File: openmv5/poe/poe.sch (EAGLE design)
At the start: 47 parts, among them IC1 AG9905LP, J1 GMJXHT-MM-S-88, T1 PT61018PEL, U1 OPENMV5-BOTTOM

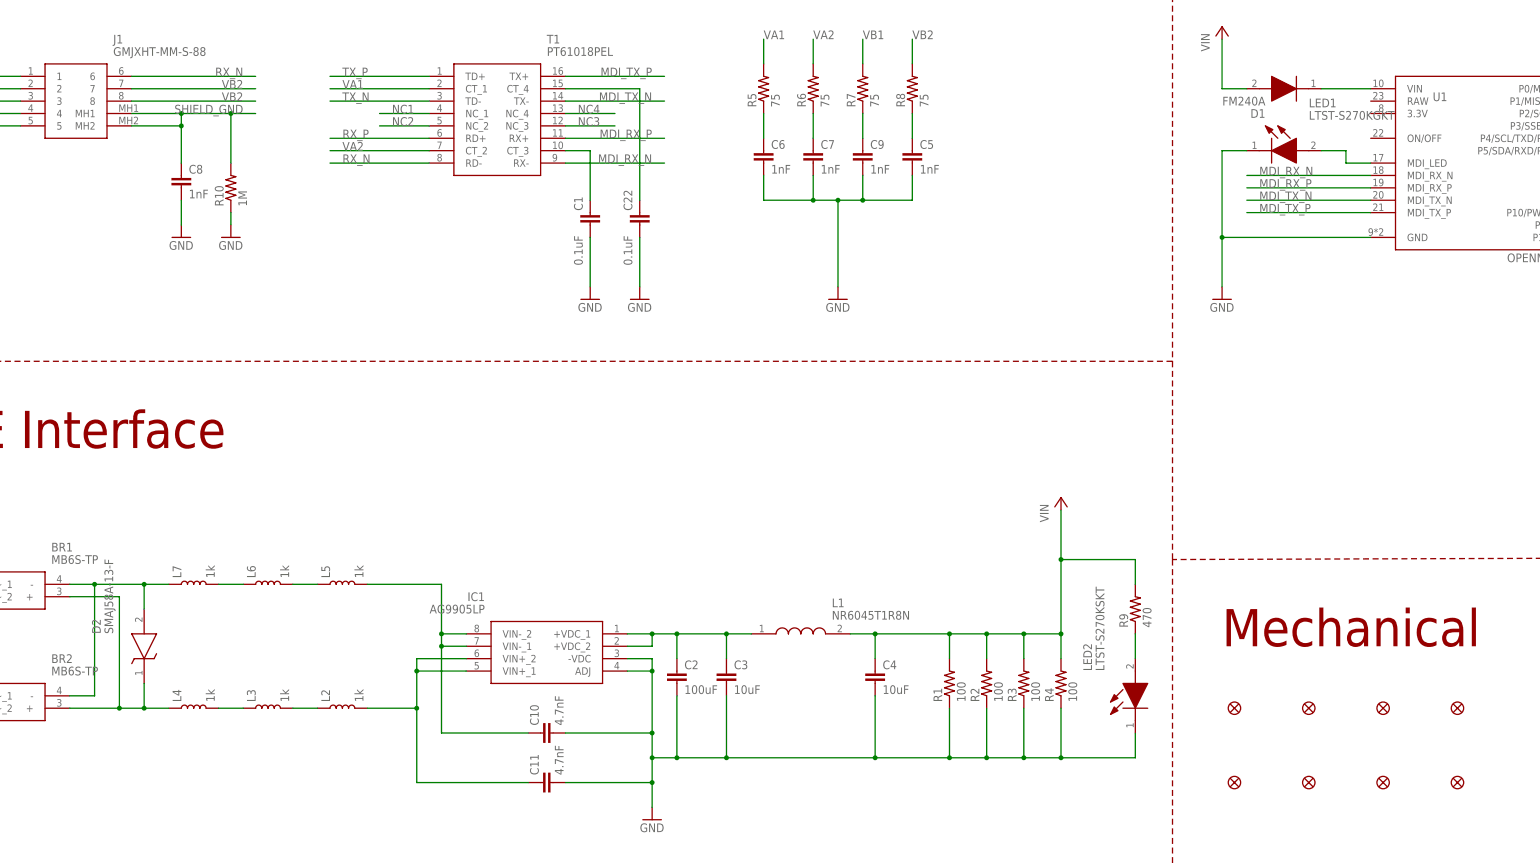
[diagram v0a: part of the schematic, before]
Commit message: Add labels to PoE shield
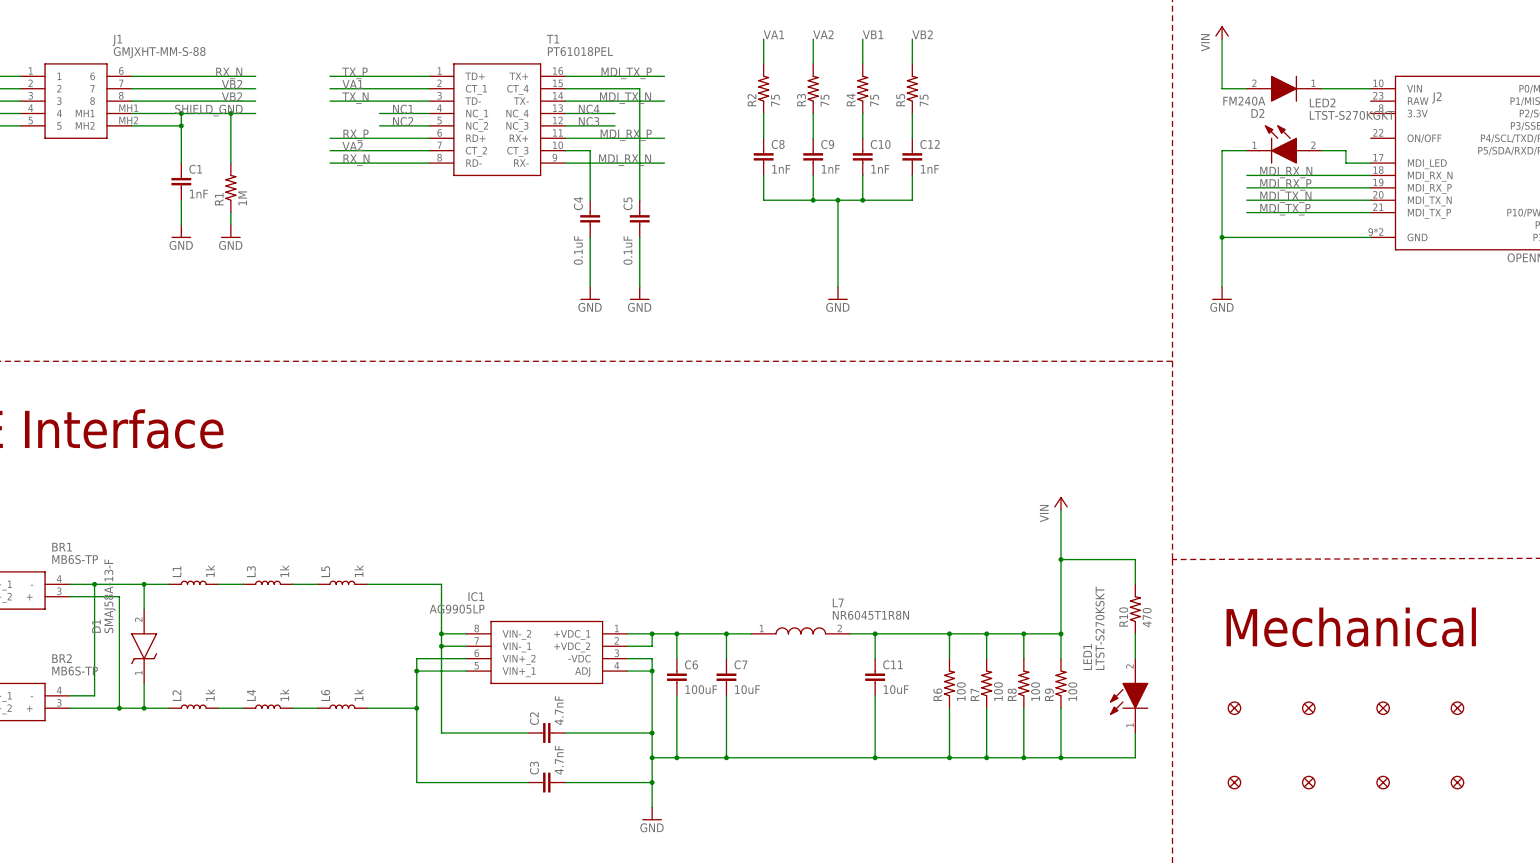
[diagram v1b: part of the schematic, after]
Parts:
- removed C22: 0.1uF, rcl:C-EUC0201
- added C12: 1nF, rcl:C-EUC1206
- C1: value 0.1uF -> 1nF; device rcl:C-EUC0201 -> rcl:C-EUC1206; MPN CL03A104KQ3NNNC -> 1206B102K252CT
- C10: value 4.7nF -> 1nF; device rcl:C-EUC1812 -> rcl:C-EUC1206; MPN 202S43W472KV4E -> 1206B102K252CT
- C11: value 4.7nF -> 10uF; device rcl:C-EUC1812 -> rcl:C-EUC0402; MPN 202S43W472KV4E -> GRM155R60J106ME05D
- C2: value 100uF -> 4.7nF; device rcl:C-EUC1206 -> rcl:C-EUC1812; MPN CL31A107MQHNNWE -> 202S43W472KV4E
- C3: value 10uF -> 4.7nF; device rcl:C-EUC0402 -> rcl:C-EUC1812; MPN GRM155R60J106ME05D -> 202S43W472KV4E
- C4: value 10uF -> 0.1uF; device rcl:C-EUC0402 -> rcl:C-EUC0201; MPN GRM155R60J106ME05D -> CL03A104KQ3NNNC
- C5: value 1nF -> 0.1uF; device rcl:C-EUC1206 -> rcl:C-EUC0201; MPN 1206B102K252CT -> CL03A104KQ3NNNC
- C6: value 1nF -> 100uF; MPN 1206B102K252CT -> CL31A107MQHNNWE
- C7: value 1nF -> 10uF; device rcl:C-EUC1206 -> rcl:C-EUC0402; MPN 1206B102K252CT -> GRM155R60J106ME05D
- D1: value FM240A -> SMAJ58A-13-F; device FM240A:FM240A -> SMAJ58A-13-F:SMAJ58A-13-F; MPN FM240A -> SMAJ58A/TR13
- D2: value SMAJ58A-13-F -> FM240A; device SMAJ58A-13-F:SMAJ58A-13-F -> FM240A:FM240A; MPN SMAJ58A/TR13 -> FM240A
- L1: value NR6045T1R8N -> 1k; device NR6045T1R8N:NR6045T1R8N -> SparkFun-Coils:INDUCTOR-0402-3.9NH; MPN NR6045T1R8N -> BBPY00100505102Y00
- L7: value 1k -> NR6045T1R8N; device SparkFun-Coils:INDUCTOR-0402-3.9NH -> NR6045T1R8N:NR6045T1R8N; MPN BBPY00100505102Y00 -> NR6045T1R8N
- LED1: value LTST-S270KGKT -> LTST-S270KSKT; device LTST-S270K:LTST-S270KGKT -> LTST-S270K:LTST-S270KSKT; MPN LTST-S270KGKT -> LTST-S270KSKT
- LED2: value LTST-S270KSKT -> LTST-S270KGKT; device LTST-S270K:LTST-S270KSKT -> LTST-S270K:LTST-S270KGKT; MPN LTST-S270KSKT -> LTST-S270KGKT
- R1: value 100 -> 1M; device rcl:R-US_R2512 -> rcl:R-US_R1206; MPN RC2512JK-07100RL -> RMCF1206FT1M00
- R10: value 1M -> 470; device rcl:R-US_R1206 -> rcl:R-US_R0603; MPN RMCF1206FT1M00 -> 0603WAJ0471T5E
- R2, R3, R4: value 100 -> 75; device rcl:R-US_R2512 -> rcl:R-US_R0402; MPN RC2512JK-07100RL -> 0402WGF750JTCE
- R6, R7, R8: value 75 -> 100; device rcl:R-US_R0402 -> rcl:R-US_R2512; MPN 0402WGF750JTCE -> RC2512JK-07100RL
- R9: value 470 -> 100; device rcl:R-US_R0603 -> rcl:R-US_R2512; MPN 0603WAJ0471T5E -> RC2512JK-07100RL
- renumbered U1 to J2
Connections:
- net GND: now also C12.2, R6.1, R7.1, R8.1, R9.1; no longer C22.2, R10.1, R2.1, R3.1, R4.1
- net MDI_LED: now also LED2.A; no longer LED1.A
- net MDI_RX_CT: now also C4.1; no longer C1.1
- net MDI_TX_CT: now also C5.1; no longer C22.1
- net POE_VIN_INT_N: now also C2.1; no longer C10.1
- net POE_VIN_INT_P: now also C3.1, L6.2; no longer C11.1, L2.2
- net POE_VIN_N: now also D1.A, L1.1; no longer D2.A, L7.1
- net POE_VIN_N0: now also L1.2, L3.1; no longer L6.1, L7.2
- net POE_VIN_N1: now also L3.2; no longer L6.2
- net POE_VIN_P: now also D1.K, L2.1; no longer D2.K, L4.1
- net POE_VIN_P0: now also L2.2, L4.1; no longer L3.1, L4.2
- net POE_VIN_P1: now also L4.2, L6.1; no longer L2.1, L3.2
- net SHIELD_GND: now also C1.1, R1.2; no longer C8.1, R10.2
- net VA1: now also R2.2; no longer R5.2
- net VA1_ISO: now also C8.1, R2.1; no longer C6.1, R5.1
- net VA2: now also R3.2; no longer R6.2
- net VA2_ISO: now also C9.1, R3.1; no longer C7.1, R6.1
- net VB1: now also R4.2; no longer R7.2
- net VB1_ISO: now also C10.1, R4.1; no longer C9.1, R7.1
- net VB2: now also R5.2; no longer R8.2
- net VB2_ISO: now also C12.1, R5.1; no longer C5.1, R8.1
- net VDC: now also C6.1, C7.1, L7.1; no longer C2.1, C3.1, L1.1
- net VIN: now also C11.1, D2.A, L7.2, R10.2, R6.2, R7.2, R8.2; no longer C4.1, D1.A, L1.2, R1.2, R2.2, R3.2, R4.2
- net VIN_INT: now also D2.K; no longer D1.K
- net VIN_LED: now also LED1.A, R10.1; no longer LED2.A, R9.1
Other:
- moved on the sheet: C1, C10, C11, C2, C3, C4, C5, C6, C7, C8, C9, L2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

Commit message: Update part
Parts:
- R10: MPN 0603WAJ0471T5E -> CR0603-FX-4700ELF
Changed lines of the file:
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@@
 </pinmapping>
 </spice>
-<attribute name="MPN" value="0603WAJ0471T5E"/>
+<attribute name="MPN" value="CR0603-FX-4700ELF"/>
 </part>
 <part name="D1" library="SMAJ58A-13-F" deviceset="SMAJ58A-13-F" device="">

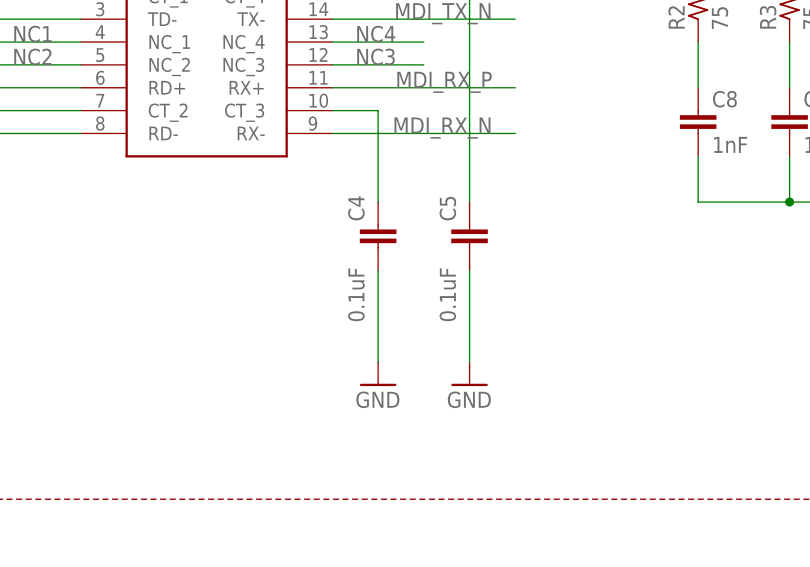
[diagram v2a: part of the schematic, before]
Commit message: Remove 0201 components
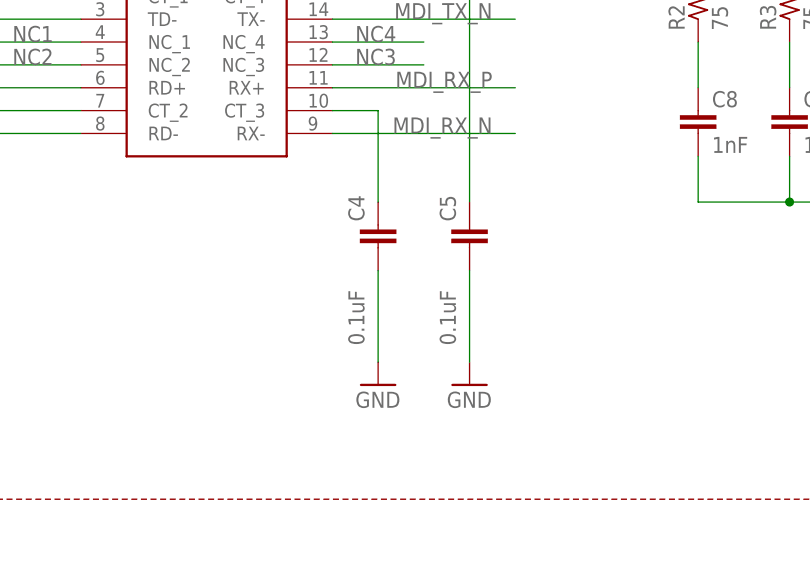
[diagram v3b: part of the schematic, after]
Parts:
- C4, C5: device rcl:C-EUC0201 -> SparkFun-Capacitors:0.1UF-0402-16V-10%; MPN CL03A104KQ3NNNC -> GRM155R71H104KE14D
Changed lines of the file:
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@@
 <attribute name="MPN" value="PT61018PEL"/>
 </part>
-<part name="C5" library="rcl" library_urn="urn:adsk.eagle:library:334" deviceset="C-EU" device="C0201" package3d_urn="urn:adsk.eagle:package:23690/2" value="0.1uF">
-<attribute name="MPN" value="CL03A104KQ3NNNC"/>
-</part>
-<part name="C4" library="rcl" library_urn="urn:adsk.eagle:library:334" deviceset="C-EU" device="C0201" package3d_urn="urn:adsk.eagle:package:23690/2" value="0.1uF">
-<attribute name="MPN" value="CL03A104KQ3NNNC"/>
+<part name="C5" library="SparkFun-Capacitors" library_urn="urn:adsk.eagle:library:510" deviceset="0.1UF" device="-0402-16V-10%" package3d_urn="urn:adsk.eagle:package:37413/1" value="0.1uF">
+<attribute name="MPN" value="GRM155R71H104KE14D"/>
+</part>
+<part name="C4" library="SparkFun-Capacitors" library_urn="urn:adsk.eagle:library:510" deviceset="0.1UF" device="-0402-16V-10%" package3d_urn="urn:adsk.eagle:package:37413/1" value="0.1uF">
+<attribute name="MPN" value="GRM155R71H104KE14D"/>
 </part>
 <part name="GND1" library="supply1" library_urn="urn:adsk.eagle:library:371" deviceset="GND" device=""/>
@@
 <attribute name="MPN" x="119.38" y="236.22" size="1.778" layer="96" display="off"/>
 </instance>
-<instance part="C5" gate="G$1" x="162.56" y="208.28" smashed="yes" rot="MR0">
+<instance part="C5" gate="G$1" x="162.56" y="205.74" smashed="yes" rot="MR0">
 <attribute name="NAME" x="161.036" y="208.661" size="1.778" layer="95" rot="R90"/>
-<attribute name="VALUE" x="161.036" y="203.581" size="1.778" layer="96" rot="MR270"/>
-<attribute name="MPN" x="162.56" y="208.28" size="1.778" layer="96" rot="MR0" display="off"/>
-</instance>
-<instance part="C4" gate="G$1" x="152.4" y="208.28" smashed="yes" rot="MR0">
+<attribute name="VALUE" x="161.036" y="201.041" size="1.778" layer="96" rot="MR270"/>
+<attribute name="MPN" x="162.56" y="205.74" size="1.778" layer="96" rot="MR0" display="off"/>
+</instance>
+<instance part="C4" gate="G$1" x="152.4" y="205.74" smashed="yes" rot="MR0">
 <attribute name="NAME" x="150.876" y="208.661" size="1.778" layer="95" rot="R90"/>
-<attribute name="VALUE" x="150.876" y="203.581" size="1.778" layer="96" rot="MR270"/>
-<attribute name="MPN" x="152.4" y="208.28" size="1.778" layer="96" rot="MR0" display="off"/>
+<attribute name="VALUE" x="150.876" y="201.041" size="1.778" layer="96" rot="MR270"/>
+<attribute name="MPN" x="152.4" y="205.74" size="1.778" layer="96" rot="MR0" display="off"/>
 </instance>
 <instance part="GND1" gate="1" x="152.4" y="190.5" smashed="yes">

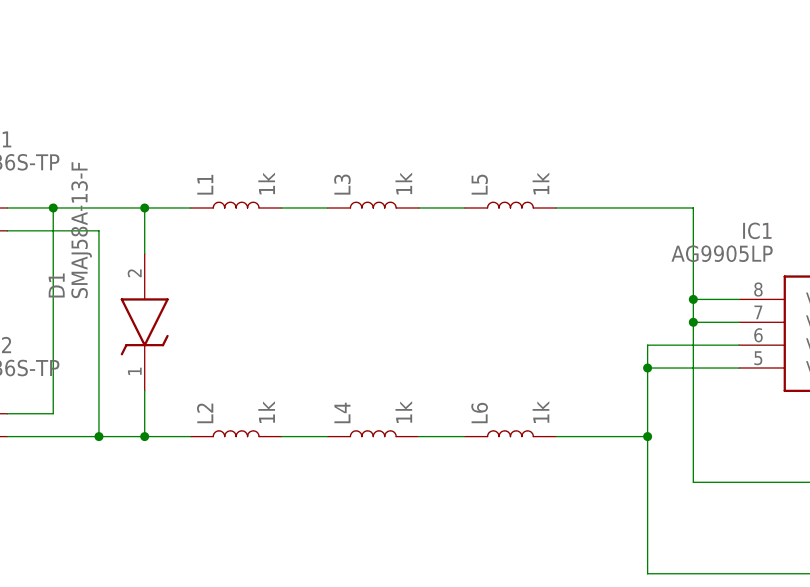
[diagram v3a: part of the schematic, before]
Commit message: Fix inductor size
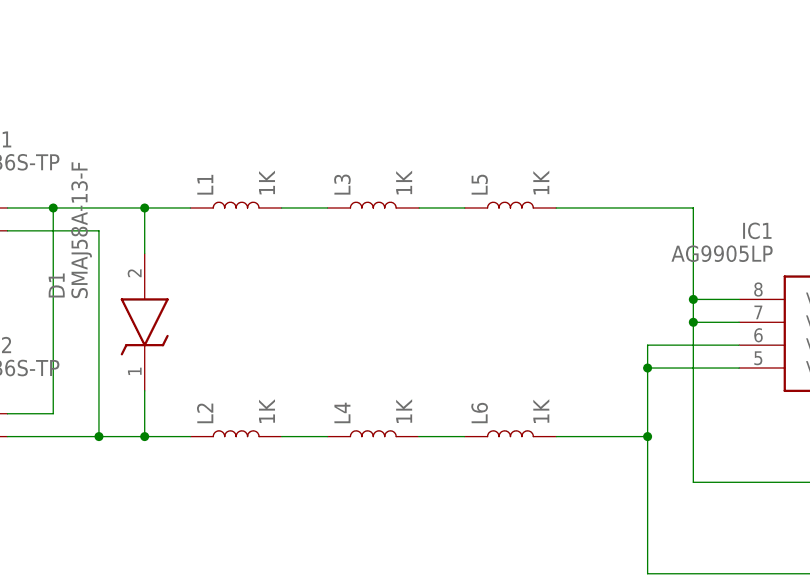
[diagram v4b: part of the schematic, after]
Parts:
- L1, L2, L3, L4, L5, L6: value 1k -> 1K; device SparkFun-Coils:INDUCTOR-0402-3.9NH -> SparkFun-Coils:INDUCTOR-0805-3.3UH
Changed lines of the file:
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@@
 <attribute name="MPN" value="202S43W472KV4E"/>
 </part>
-<part name="L6" library="SparkFun-Coils" library_urn="urn:adsk.eagle:library:512" deviceset="INDUCTOR" device="-0402-3.9NH" package3d_urn="urn:adsk.eagle:package:37575/1" value="1k">
+<part name="L6" library="SparkFun-Coils" library_urn="urn:adsk.eagle:library:512" deviceset="INDUCTOR" device="-0805-3.3UH" package3d_urn="urn:adsk.eagle:package:37579/1" value="1K">
 <attribute name="MPN" value="BBPY00100505102Y00"/>
 </part>
-<part name="L4" library="SparkFun-Coils" library_urn="urn:adsk.eagle:library:512" deviceset="INDUCTOR" device="-0402-3.9NH" package3d_urn="urn:adsk.eagle:package:37575/1" value="1k">
+<part name="L4" library="SparkFun-Coils" library_urn="urn:adsk.eagle:library:512" deviceset="INDUCTOR" device="-0805-3.3UH" package3d_urn="urn:adsk.eagle:package:37579/1" value="1K">
 <attribute name="MPN" value="BBPY00100505102Y00"/>
 </part>
-<part name="L2" library="SparkFun-Coils" library_urn="urn:adsk.eagle:library:512" deviceset="INDUCTOR" device="-0402-3.9NH" package3d_urn="urn:adsk.eagle:package:37575/1" value="1k">
+<part name="L2" library="SparkFun-Coils" library_urn="urn:adsk.eagle:library:512" deviceset="INDUCTOR" device="-0805-3.3UH" package3d_urn="urn:adsk.eagle:package:37579/1" value="1K">
 <attribute name="MPN" value="BBPY00100505102Y00"/>
 </part>
-<part name="L5" library="SparkFun-Coils" library_urn="urn:adsk.eagle:library:512" deviceset="INDUCTOR" device="-0402-3.9NH" package3d_urn="urn:adsk.eagle:package:37575/1" value="1k">
+<part name="L5" library="SparkFun-Coils" library_urn="urn:adsk.eagle:library:512" deviceset="INDUCTOR" device="-0805-3.3UH" package3d_urn="urn:adsk.eagle:package:37579/1" value="1K">
 <attribute name="MPN" value="BBPY00100505102Y00"/>
 </part>
-<part name="L3" library="SparkFun-Coils" library_urn="urn:adsk.eagle:library:512" deviceset="INDUCTOR" device="-0402-3.9NH" package3d_urn="urn:adsk.eagle:package:37575/1" value="1k">
+<part name="L3" library="SparkFun-Coils" library_urn="urn:adsk.eagle:library:512" deviceset="INDUCTOR" device="-0805-3.3UH" package3d_urn="urn:adsk.eagle:package:37579/1" value="1K">
 <attribute name="MPN" value="BBPY00100505102Y00"/>
 </part>
-<part name="L1" library="SparkFun-Coils" library_urn="urn:adsk.eagle:library:512" deviceset="INDUCTOR" device="-0402-3.9NH" package3d_urn="urn:adsk.eagle:package:37575/1" value="1k">
+<part name="L1" library="SparkFun-Coils" library_urn="urn:adsk.eagle:library:512" deviceset="INDUCTOR" device="-0805-3.3UH" package3d_urn="urn:adsk.eagle:package:37579/1" value="1K">
 <attribute name="MPN" value="BBPY00100505102Y00"/>
 </part>

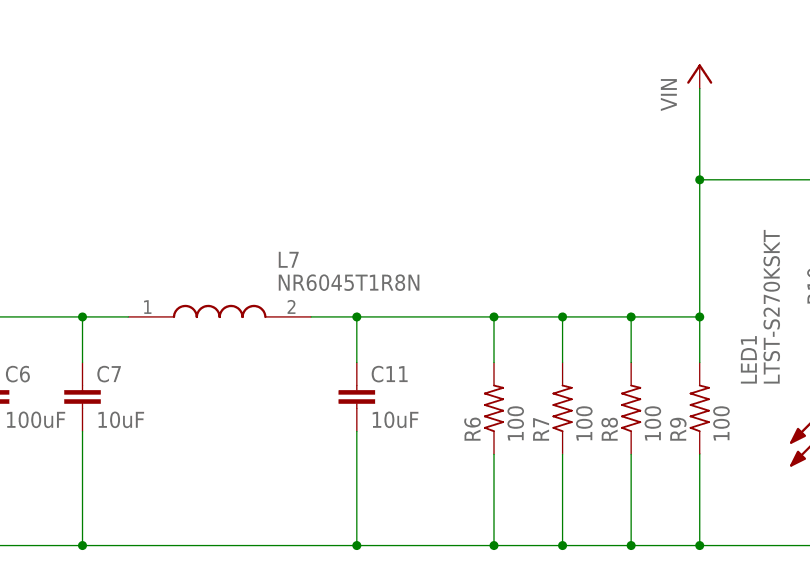
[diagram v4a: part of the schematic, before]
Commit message: Change inductor to something smaller
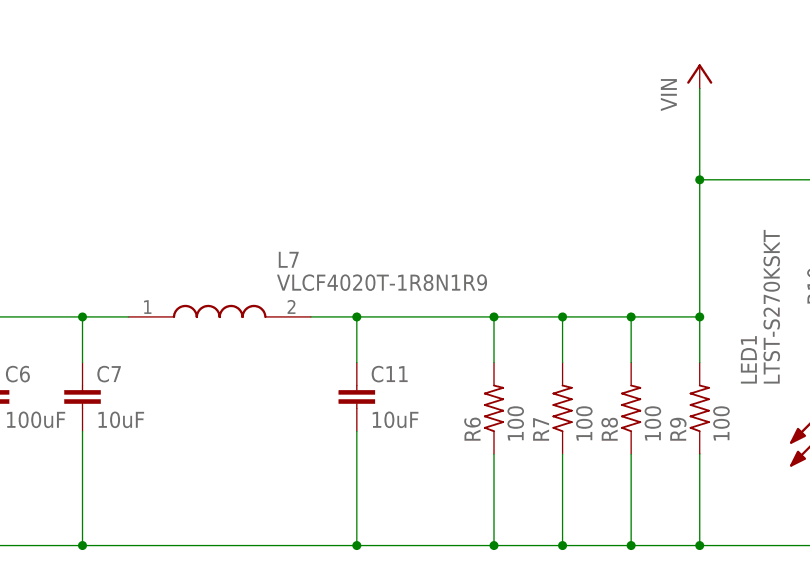
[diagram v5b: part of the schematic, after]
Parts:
- L7: value NR6045T1R8N -> VLCF4020T-1R8N1R9; device NR6045T1R8N:NR6045T1R8N -> VLCF4020T-1R8N1R9:VLCF4020T-1R8N1R9; MPN NR6045T1R8N -> VLCF4020T-1R8N1R9
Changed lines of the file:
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@@
 </part>
 <part name="GND3" library="supply1" library_urn="urn:adsk.eagle:library:371" deviceset="GND" device=""/>
-<part name="L7" library="NR6045T1R8N" deviceset="NR6045T1R8N" device="">
-<attribute name="MPN" value="NR6045T1R8N"/>
+<part name="L7" library="VLCF4020T-1R8N1R9" deviceset="VLCF4020T-1R8N1R9" device="">
+<attribute name="MPN" value="VLCF4020T-1R8N1R9"/>
 </part>
 <part name="C7" library="rcl" library_urn="urn:adsk.eagle:library:334" deviceset="C-EU" device="C0402" package3d_urn="urn:adsk.eagle:package:23626/2" value="10uF">

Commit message: Fix part and add 3D
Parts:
- R2, R3, R4, R5: MPN 0402WGF750JTCE -> CR0402-FX-75R0GLF
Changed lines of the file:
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@@
 </pinmapping>
 </spice>
-<attribute name="MPN" value="0402WGF750JTCE"/>
+<attribute name="MPN" value="CR0402-FX-75R0GLF"/>
 </part>
 <part name="R3" library="rcl" library_urn="urn:adsk.eagle:library:334" deviceset="R-US_" device="R0402" package3d_urn="urn:adsk.eagle:package:23547/3" value="75">
@@
 </pinmapping>
 </spice>
-<attribute name="MPN" value="0402WGF750JTCE"/>
+<attribute name="MPN" value="CR0402-FX-75R0GLF"/>
 </part>
 <part name="R4" library="rcl" library_urn="urn:adsk.eagle:library:334" deviceset="R-US_" device="R0402" package3d_urn="urn:adsk.eagle:package:23547/3" value="75">
@@
 </pinmapping>
 </spice>
-<attribute name="MPN" value="0402WGF750JTCE"/>
+<attribute name="MPN" value="CR0402-FX-75R0GLF"/>
 </part>
 <part name="R5" library="rcl" library_urn="urn:adsk.eagle:library:334" deviceset="R-US_" device="R0402" package3d_urn="urn:adsk.eagle:package:23547/3" value="75">
@@
 </pinmapping>
 </spice>
-<attribute name="MPN" value="0402WGF750JTCE"/>
+<attribute name="MPN" value="CR0402-FX-75R0GLF"/>
 </part>
 <part name="C10" library="rcl" library_urn="urn:adsk.eagle:library:334" deviceset="C-EU" device="C1206" package3d_urn="urn:adsk.eagle:package:23618/2" value="1nF">
